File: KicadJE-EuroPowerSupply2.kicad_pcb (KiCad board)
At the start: 2 copper layers, 159 x 128 mm, 143 parts, among them J101 Laptop Power, J102 +-15V thru, J103 +-12v out, J104 +5V out, J105 Laptop Power Out, J106 FrontInterConnVin, J107 FrontInterConnVin, J108 Conn_01x08, J109 Conn_01x08, P101 Doepfer_Power_10pin, P102 Doepfer_Power_16pin, P105 Doepfer_Power_10pin, P106 Doepfer_Power_16pin, Q201 TIP41, Q202 TIP41, Q203 TIP42, Q204 MMBT2907A, Q205 MMBT2222A, Q206 MMBT2907A, SW101 SW_SPDT, U201 LM7812_TO220, U202 LM7805_TO220, U203 Step Down Module +15 to 7v - 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, U204 LM7912_TO220, U205 XL6009 Module DCDC 19 to 30v, U206 TL071, U207 LM78M05_TO252, U208 LM78M12_TO252, U209 MC79M12_TO252

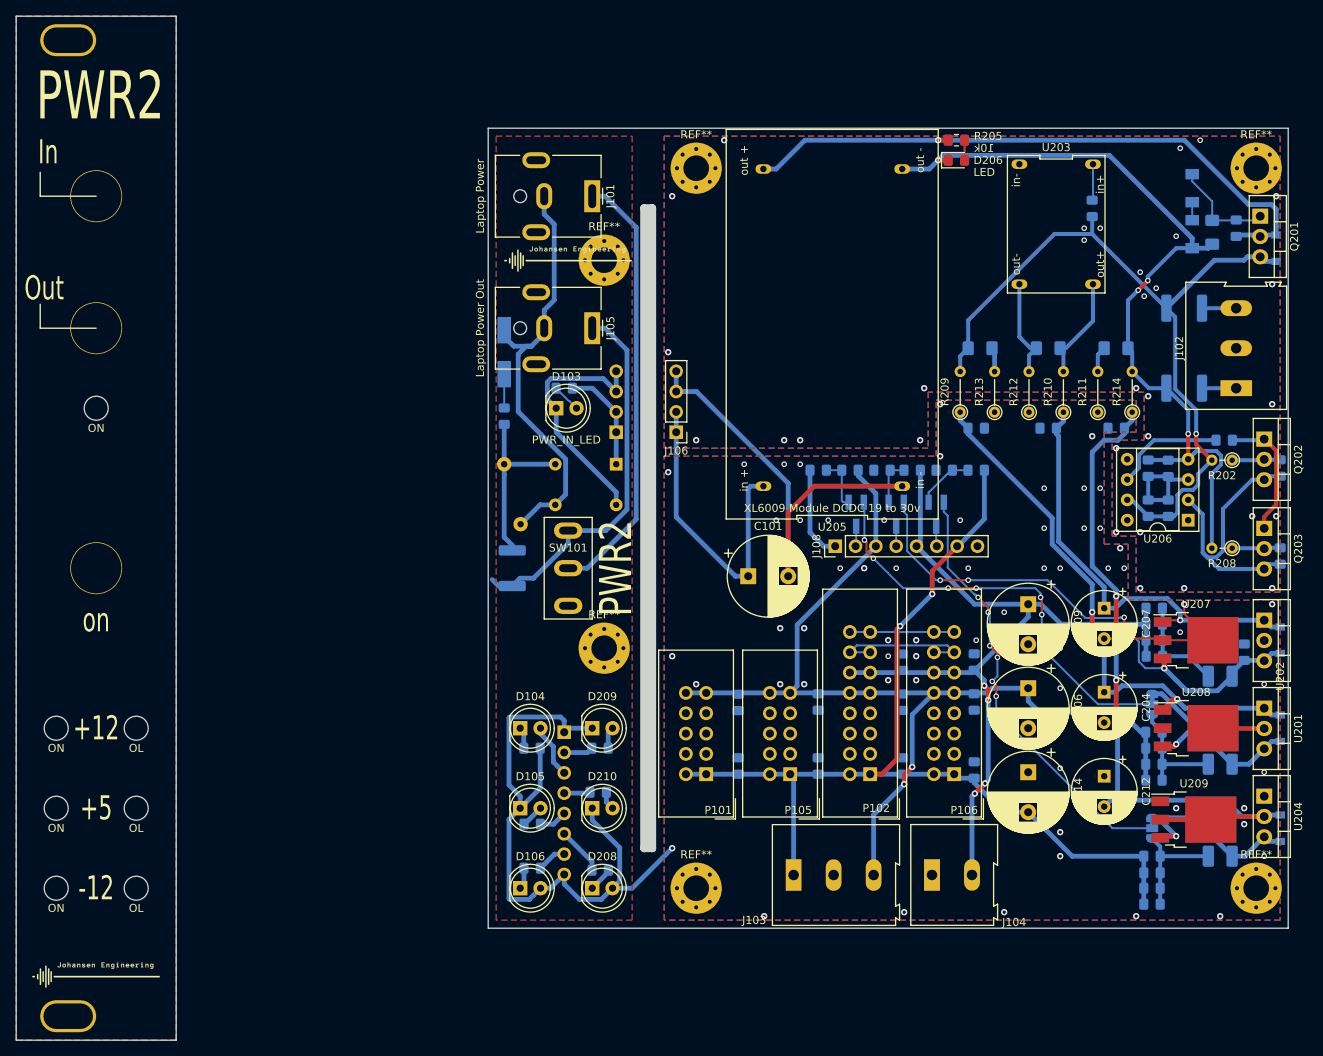
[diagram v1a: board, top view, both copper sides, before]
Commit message: Update KicadJE-EuroPowerSupply2.kicad_pcb
DRC + Labels
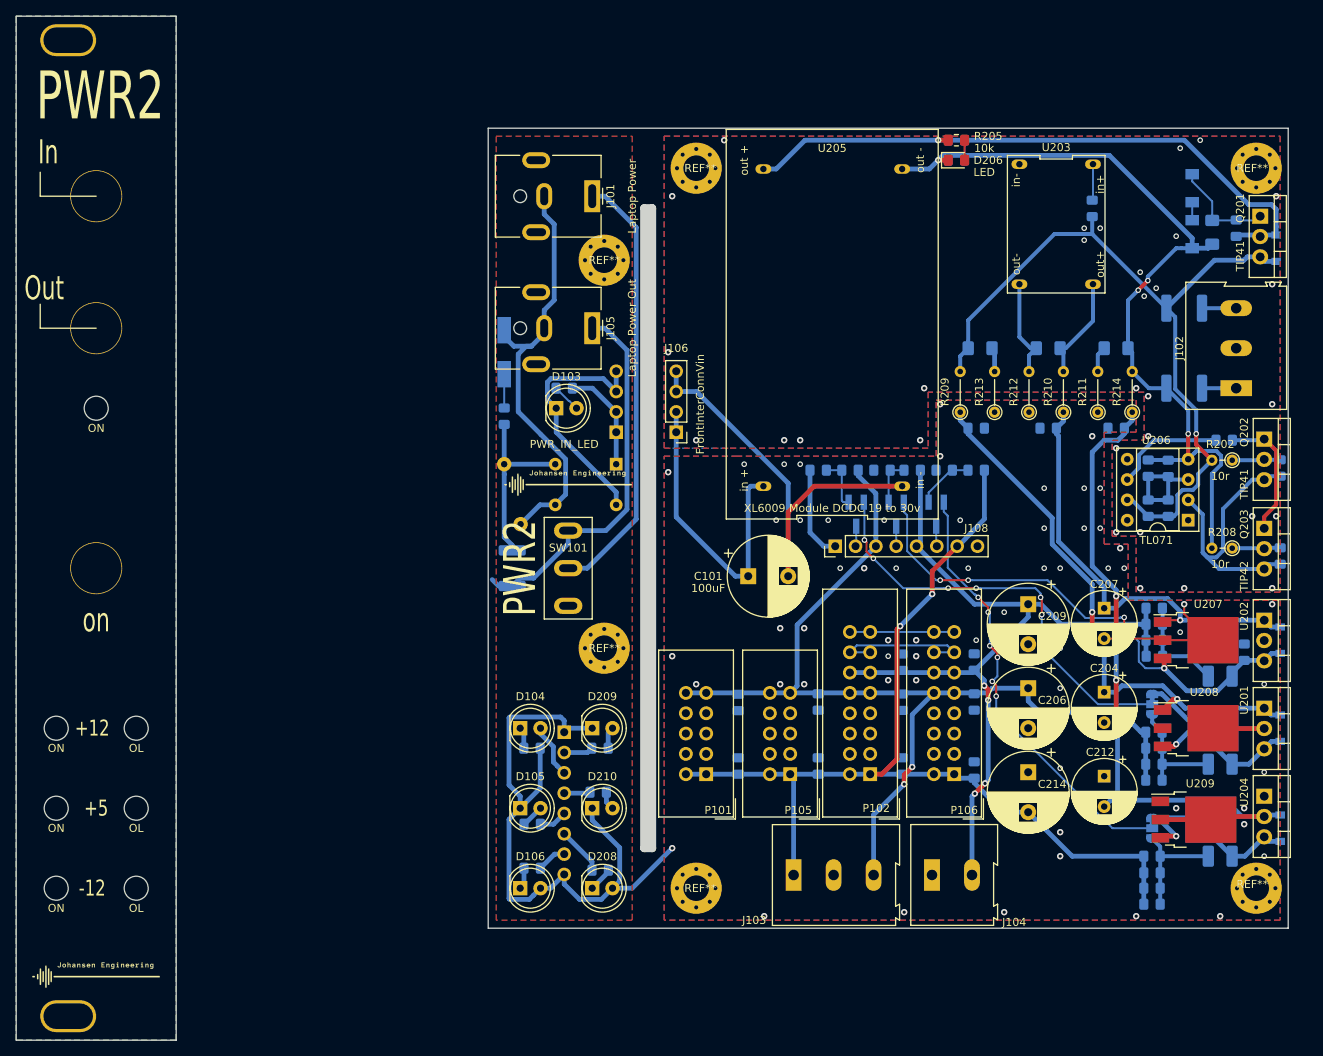
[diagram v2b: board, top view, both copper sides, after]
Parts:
- moved G*** 28.0 mm to (60.0, 94.5)
